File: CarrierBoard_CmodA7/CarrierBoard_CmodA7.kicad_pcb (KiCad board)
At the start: 2 copper layers, 76 x 85 mm, 69 parts, among them CN1 Mini-Fit_Jr._Header,_2_Circui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, J2 Conn1x26, U1 AZ1084CD-5.0, U2 Cmod_A7, U3 PMOD_GPIO, U4 PMOD_GPIO, U5 PMOD_GPIO, U6 PMOD_GPIO, U7 Conn1x21

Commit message: Arreglado Tira pines 1x22 a 1x21, cambiado el nivel de prioridad de los planos de cobre
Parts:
- U7: footprint Connector_PinSocket_2.54mm:PinSocket_1x22_P2.54mm_Vertical -> Connector_PinSocket_2.54mm:PinSocket_1x21_P2.54mm_Vertical
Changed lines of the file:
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@@
     )
   )
-  (footprint "Connector_PinSocket_2.54mm:PinSocket_1x22_P2.54mm_Vertical" (layer "F.Cu")
+  (footprint "Connector_PinSocket_2.54mm:PinSocket_1x21_P2.54mm_Vertical" (layer "F.Cu")
     (at 188.37 103.6 180)
-    (descr "Through hole straight socket strip, 1x22, 2.54mm pitch, single row (from Kicad 4.0.7), script generated")
-    (tags "Through hole socket strip THT 1x22 2.54mm single row")
+    (descr "Through hole straight socket strip, 1x21, 2.54mm pitch, single row (from Kicad 4.0.7), script generated")
+    (tags "Through hole socket strip THT 1x21 2.54mm single row")
     (property "Sheetfile" "CarrierBoard_CmodA7.kicad_sch")
     (property "Sheetname" "")
     (attr through_hole)
-    (fp_text reference "U7" (at 0 -2.77) (layer "F.SilkS")
-      (effects (font (size 1 1) (thickness 0.15)))
-    )
-    (fp_text value "Conn1x21" (at 0 56.11) (layer "F.Fab")
-      (effects (font (size 1 1) (thickness 0.15)))
-    )
-    (fp_text user "${REFERENCE}" (at 0 26.67 90) (layer "F.Fab")
+    (fp_text reference "U7" (at 0 -2.77 180) (layer "F.SilkS")
+      (effects (font (size 1 1) (thickness 0.15)))
+    )
+    (fp_text value "Conn1x21" (at 0 53.57 180) (layer "F.Fab")
+      (effects (font (size 1 1) (thickness 0.15)))
+    )
+    (fp_text user "${REFERENCE}" (at 0 25.4 270) (layer "F.Fab")
       (effects (font (size 1 1) (thickness 0.15)))
     )
     (fp_line (start 1.33 -1.33) (end 1.33 0) (layer "F.SilkS") (width 0.12))
+    (fp_line (start 0 -1.33) (end 1.33 -1.33) (layer "F.SilkS") (width 0.12))
+    (fp_line (start -1.33 1.27) (end -1.33 52.13) (layer "F.SilkS") (width 0.12))
+    (fp_line (start 1.33 1.27) (end 1.33 52.13) (layer "F.SilkS") (width 0.12))
     (fp_line (start -1.33 1.27) (end 1.33 1.27) (layer "F.SilkS") (width 0.12))
-    (fp_line (start 1.33 1.27) (end 1.33 54.67) (layer "F.SilkS") (width 0.12))
-    (fp_line (start 0 -1.33) (end 1.33 -1.33) (layer "F.SilkS") (width 0.12))
-    (fp_line (start -1.33 1.27) (end -1.33 54.67) (layer "F.SilkS") (width 0.12))
-    (fp_line (start -1.33 54.67) (end 1.33 54.67) (layer "F.SilkS") (width 0.12))
+    (fp_line (start -1.33 52.13) (end 1.33 52.13) (layer "F.SilkS") (width 0.12))
+    (fp_line (start 1.75 52.55) (end -1.8 52.55) (layer "F.CrtYd") (width 0.05))
     (fp_line (start -1.8 -1.8) (end 1.75 -1.8) (layer "F.CrtYd") (width 0.05))
-    (fp_line (start 1.75 55.1) (end -1.8 55.1) (layer "F.CrtYd") (width 0.05))
-    (fp_line (start 1.75 -1.8) (end 1.75 55.1) (layer "F.CrtYd") (width 0.05))
-    (fp_line (start -1.8 55.1) (end -1.8 -1.8) (layer "F.CrtYd") (width 0.05))
-    (fp_line (start -1.27 54.61) (end -1.27 -1.27) (layer "F.Fab") (width 0.1))
-    (fp_line (start 1.27 -0.635) (end 1.27 54.61) (layer "F.Fab") (width 0.1))
+    (fp_line (start -1.8 52.55) (end -1.8 -1.8) (layer "F.CrtYd") (width 0.05))
+    (fp_line (start 1.75 -1.8) (end 1.75 52.55) (layer "F.CrtYd") (width 0.05))
+    (fp_line (start 1.27 -0.635) (end 1.27 52.07) (layer "F.Fab") (width 0.1))
+    (fp_line (start 1.27 52.07) (end -1.27 52.07) (layer "F.Fab") (width 0.1))
+    (fp_line (start -1.27 52.07) (end -1.27 -1.27) (layer "F.Fab") (width 0.1))
+    (fp_line (start -1.27 -1.27) (end 0.635 -1.27) (layer "F.Fab") (width 0.1))
     (fp_line (start 0.635 -1.27) (end 1.27 -0.635) (layer "F.Fab") (width 0.1))
-    (fp_line (start 1.27 54.61) (end -1.27 54.61) (layer "F.Fab") (width 0.1))
-    (fp_line (start -1.27 -1.27) (end 0.635 -1.27) (layer "F.Fab") (width 0.1))
     (pad "1" thru_hole rect (at 0 0 180) (size 1.7 1.7) (drill 1) (layers *.Cu *.Mask)
       (net 6 "/IO1") (pinfunction "Pin_1") (pintype "passive"))
@@
     (pad "21" thru_hole oval (at 0 50.8 180) (size 1.7 1.7) (drill 1) (layers *.Cu *.Mask)
       (net 26 "/IO23") (pinfunction "Pin_21") (pintype "passive"))
-    (pad "22" thru_hole oval (at 0 53.34 180) (size 1.7 1.7) (drill 1) (layers *.Cu *.Mask))
-    (model "${KICAD6_3DMODEL_DIR}/Connector_PinSocket_2.54mm.3dshapes/PinSocket_1x22_P2.54mm_Vertical.wrl"
+    (model "${KICAD6_3DMODEL_DIR}/Connector_PinSocket_2.54mm.3dshapes/PinSocket_1x21_P2.54mm_Vertical.wrl"
       (offset (xyz 0 0 0))
       (scale (xyz 1 1 1))
@@
   )
   (zone (net 3) (net_name "+5VP") (layers F&B.Cu) (name "Thermal_Pad_Reg") (hatch edge 0.508)
+    (priority 1)
     (connect_pads yes (clearance 0.508))
     (min_thickness 0.254) (filled_areas_thickness no)
@@
     )
   )
-  (group "" (id b1729f9a-6241-4cf6-bc53-ffd2bc28c323)
-    (members
-      0e0ad59f-49c7-49e1-8181-4f4bccf85da4
-      0eba42d8-d7ba-40e9-9f63-a692f6ebec70
-      22800718-21a1-4d16-a6ef-62ea4e1a25d2
-      259f3bbe-b5fe-4a23-b8a5-4151f1c52b79
-      2838b2fd-e237-43d0-b648-62eafe5d8ba2
-      291f6aa0-1358-42fe-9954-b89ccd2c5246
-      29fa5c70-dc13-4d69-be92-fc44dbc9c06c
-      2a043446-b594-46bd-95f7-946ae3461b73
-      2a619e60-9cf4-4215-ac9c-6cd9b6a85a7e
-      360eba60-494e-4a5f-9bb9-79cd80a72cb8
-      40fa11de-0076-4b71-a33b-6abe07dfba23
-      7ce0ae94-595d-4e21-b198-de08b16fa989
-      8326c5bf-d461-4c7d-87c5-b33468c4e0e4
-      840035f9-760e-43d8-b42b-f557a49cae69
-      9749f2ba-8586-4a65-a776-3b84b130c532
-      9d6a82c1-0f4d-4bae-870a-6ea72ab488c3
-      bf55b3d2-0364-4479-8720-1aca56d25285
-      c7d1103e-0a6d-405e-84ef-a52ffdff7b0c
-      cd40a747-bd6a-4a01-aa00-0431b3021683
-      ce5b2749-5cdb-4128-9060-4f46bb280b28
-      d222c6dd-a6f9-4b4d-bd5a-f44cc391b25d
-      da97d51f-8207-40f6-b339-acda528d632e
-      dce1db7d-e8f9-4a59-b7c6-c640a8fc7761
-      e11136ec-0e76-4440-9929-ac565c57a1a3
-      e45e1b71-b8f0-4ba7-96b8-a7927cb62672
-      e6641f30-3cc7-49ac-bed5-4cb984494837
-      f2884391-266a-4503-8213-a5b50a2565c7
-      ff6428e0-e9e5-433c-ae23-83f42c1ecf89
-    )
-  )

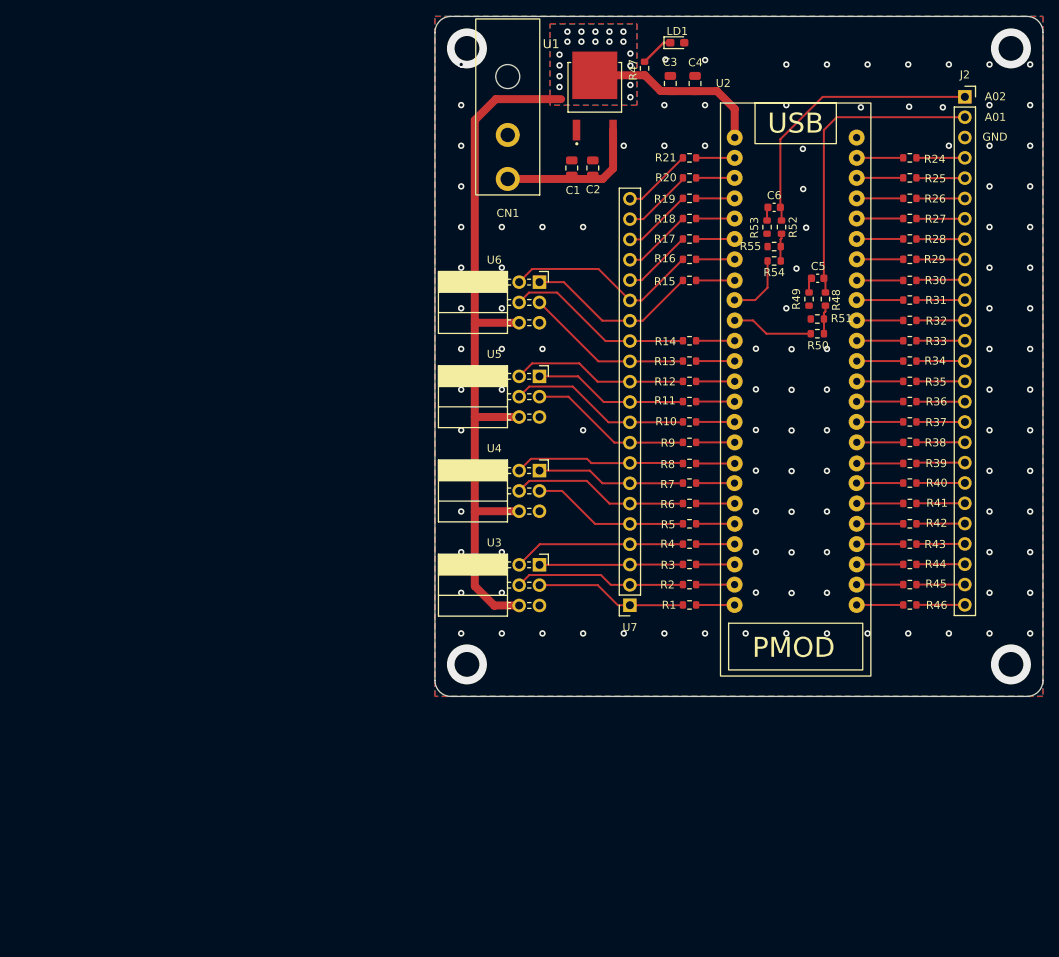
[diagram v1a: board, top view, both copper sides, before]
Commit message: arreglado divisor de tension y filtro del ADC.
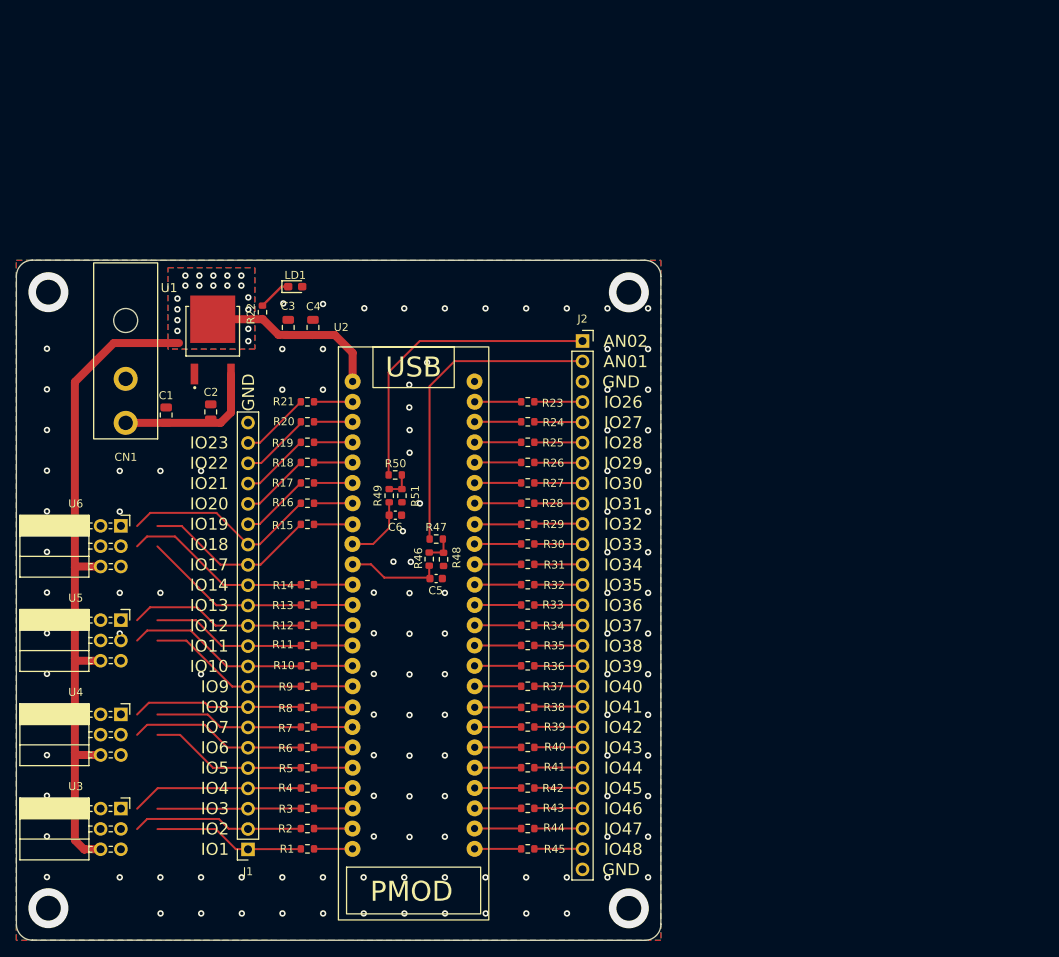
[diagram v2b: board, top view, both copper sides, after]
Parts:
- removed the R49 at (210.8, 65.3)
- removed R53: 845_P, Resistor_SMD:R_0603_1608Metric
- removed U7: Conn1x21, Connector_PinSocket_2.54mm:PinSocket_1x21_P2.54mm_Vertical
- added J1: Conn1x22, Connector_PinSocket_2.54mm:PinSocket_1x22_P2.54mm_Vertical, F.Cu at (140.6, 134.1)
- C1, C3: value 10uF -> Gen_C
- C2, C4: value 22uF -> Gen_C
- C5, C6: value 1nF -> Gen_C
- J2: value Conn1x26 -> Conn1x27; footprint Connector_PinSocket_2.54mm:PinSocket_1x26_P2.54mm_Vertical -> Connector_PinSocket_2.54mm:PinSocket_1x27_P2.54mm_Vertical
- moved C6 61.0 mm to (159.1, 92.3), turned to 0 degrees
- moved C5 60.7 mm to (164.2, 100.3), turned to 0 degrees
- moved U3 60.5 mm to (124.7, 129.0)
- moved U4 60.5 mm to (124.7, 117.2)
- moved U5 60.5 mm to (124.7, 105.5)
- moved U6 60.5 mm to (124.7, 93.7)
- moved R49 59.4 mm to (158.3, 89.9), turned to 90 degrees
- moved C1 59.4 mm to (130.4, 79.8)
- moved R46 59.2 mm to (163.3, 97.8), turned to 90 degrees
- moved J2 56.7 mm to (182.4, 70.6)
- moved R30 56.7 mm to (175.6, 95.9)
- moved R31 56.7 mm to (175.6, 98.5)
- moved R33 56.7 mm to (175.6, 103.6)
- moved R36 56.7 mm to (175.6, 111.2)
- moved R41 56.7 mm to (175.6, 123.9)
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- renumbered R47 to R22, R24 to R23, R25 to R24, R26 to R25, R27 to R26, R28 to R27, R29 to R28, R30 to R29, R31 to R30, R32 to R31, R33 to R32, R34 to R33, R35 to R34, R36 to R35, R37 to R36, R38 to R37, R39 to R38, R40 to R39, R41 to R40, R42 to R41, R43 to R42, R44 to R43, R45 to R44, R46 to R45, R48 to R46, R50 to R47, R51 to R48, R52 to R49, R54 to R50, R55 to R51
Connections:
- C5 pad 1: /AN01 -> /CH_A01
- C6 pad 1: /AN02 -> /CH_A02
- R46 pad 1: /AN01 -> /CH_A01
- R47 pad 2: /CH_A01 -> /AN01
- R49 pad 1: /AN02 -> /CH_A02
- R50 pad 2: /CH_A02 -> /AN02
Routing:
- net +5VP: track 116.2 -> 108.6 mm
- net GND: track 3.59 -> 0.00 mm, vias 116 -> 121
- net /AN02: track 35.5 -> 38.7 mm
- net /CH_A01: track 10.2 -> 12.0 mm
- net /AN01: track 38.7 -> 39.3 mm
- net /CH_A02: track 8.12 -> 8.63 mm
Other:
- board size 76 x 85 mm -> 80.6 x 85 mm
- board text added: "AN01"
- board text added: "AN02"
- board text added: "IO1"
- board text added: "IO10"
- board text added: "IO11"
- board text added: "IO12"
- board text added: "IO13"
- board text added: "IO14"
- board text added: "IO17"
- board text added: "IO18"
- board text added: "IO19"
- board text added: "IO2"
- board text added: "IO20"
- board text added: "IO21"
- board text added: "IO22"
- board text added: "IO23"
- board text added: "IO26"
- board text added: "IO27"
- board text added: "IO28"
- board text added: "IO29"
- board text added: "IO3"
- board text added: "IO30"
- board text added: "IO31"
- board text added: "IO32"
- board text added: "IO33"
- board text added: "IO34"
- board text added: "IO35"
- board text added: "IO36"
- board text added: "IO37"
- board text added: "IO38"
- board text added: "IO39"
- board text added: "IO4"
- board text added: "IO40"
- board text added: "IO41"
- board text added: "IO42"
- board text added: "IO43"
- board text added: "IO44"
- board text added: "IO45"
- board text added: "IO46"
- board text added: "IO47"
- board text added: "IO48"
- board text added: "IO5"
- board text added: "IO6"
- board text added: "IO7"
- board text added: "IO8"
- board text added: "IO9"
- board text removed: "A01"
- board text removed: "A02"

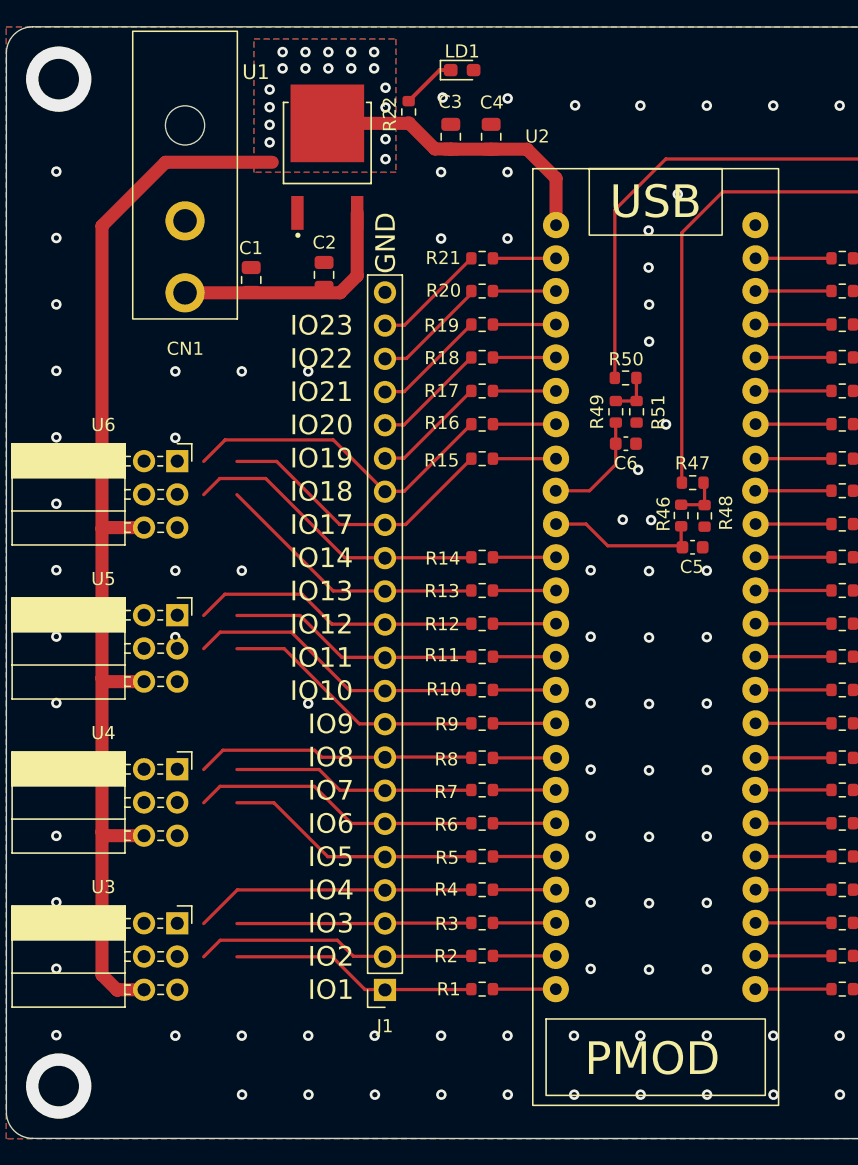
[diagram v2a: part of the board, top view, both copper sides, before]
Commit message: Retoques en la PCB, añadido info sobre el proyecto
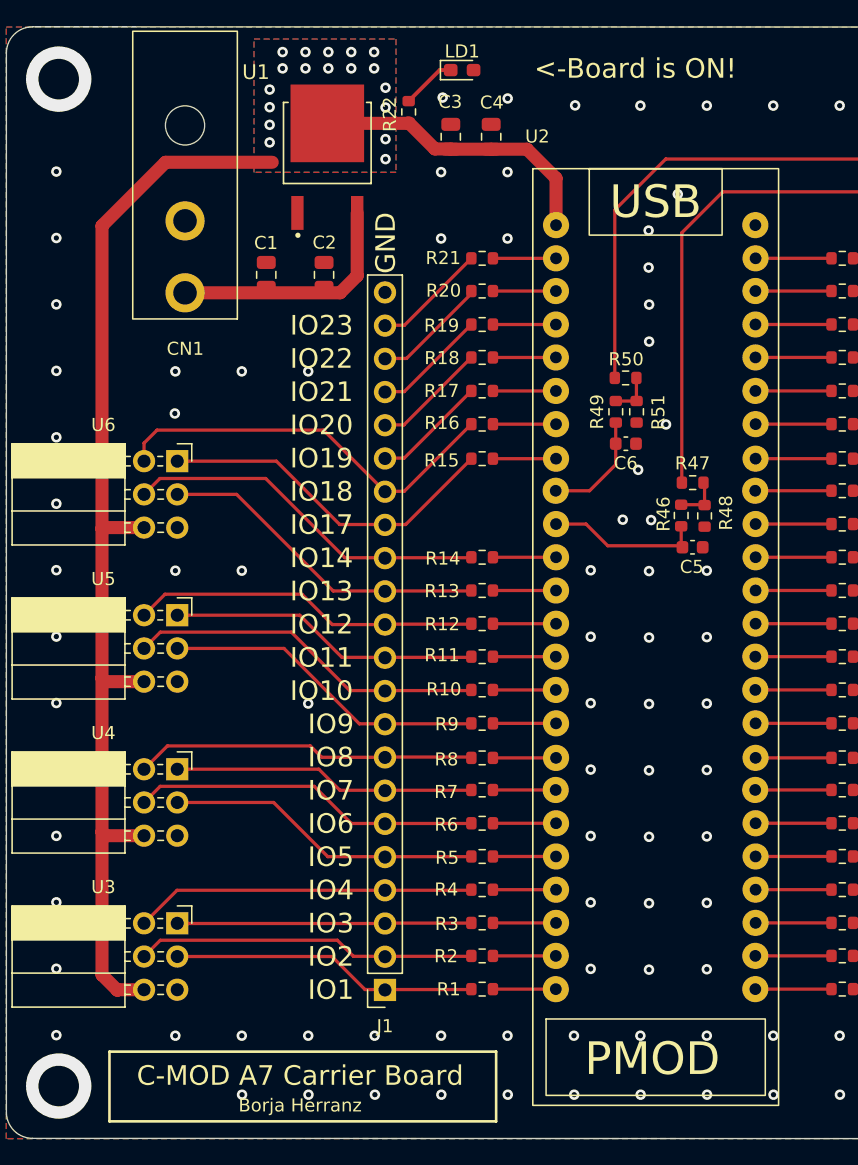
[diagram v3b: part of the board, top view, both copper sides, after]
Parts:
- moved C1 1.21 mm to (131.6, 79.4)
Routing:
- net /IO18: track 24.9 -> 30.9 mm
- net /IO8: track 21.3 -> 26.2 mm
- net /IO3: track 18.0 -> 22.6 mm
- net /IO12: track 22.8 -> 27.4 mm
- net /IO7: track 18.6 -> 23.2 mm
- net /IO5: track 19.6 -> 24.2 mm
- net /IO9: track 20.3 -> 24.9 mm
- net /IO1: track 19.0 -> 23.5 mm
- net /IO13: track 21.0 -> 25.6 mm
- net /IO11: track 19.3 -> 23.8 mm
- net /IO17: track 22.0 -> 26.6 mm
- net /IO4: track 21.5 -> 26.1 mm
- net /IO6: track 22.2 -> 26.7 mm
- net /IO2: track 21.5 -> 26.1 mm
- net /IO14: track 23.5 -> 28.1 mm
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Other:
- board text added: "<-Board is ON!"
- board text added: "Borja Herranz"
- board text added: "https://github.com/herranz/CmodA7_CarrierBoard"

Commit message: Arreglado BoM y esquemas
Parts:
- C1, C3: value Gen_C -> 10uF
- C2, C4: value Gen_C -> 100nF
- C5, C6: value Gen_C -> 1nF
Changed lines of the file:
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@@
       (effects (font (size 1 1) (thickness 0.15)))
     )
-    (fp_text value "Gen_C" (at 0 1.43) (layer "F.Fab")
+    (fp_text value "1nF" (at 0 1.43) (layer "F.Fab")
       (effects (font (size 1 1) (thickness 0.15)))
     )
@@
       (effects (font (size 1 1) (thickness 0.15)))
     )
-    (fp_text value "Gen_C" (at 0 1.68 90) (layer "F.Fab")
+    (fp_text value "100nF" (at 0 1.68 90) (layer "F.Fab")
       (effects (font (size 1 1) (thickness 0.15)))
     )
@@
       (effects (font (size 1 1) (thickness 0.15)))
     )
-    (fp_text value "Gen_C" (at 0 1.68 90) (layer "F.Fab")
+    (fp_text value "10uF" (at 0 1.68 90) (layer "F.Fab")
       (effects (font (size 1 1) (thickness 0.15)))
     )
@@
       (effects (font (size 1 1) (thickness 0.15)))
     )
-    (fp_text value "Gen_C" (at 0 1.68 90) (layer "F.Fab")
+    (fp_text value "100nF" (at 0 1.68 90) (layer "F.Fab")
       (effects (font (size 1 1) (thickness 0.15)))
     )
@@
       (effects (font (size 1 1) (thickness 0.15)))
     )
-    (fp_text value "Gen_C" (at 0 1.68 90) (layer "F.Fab")
+    (fp_text value "10uF" (at 0 1.68 90) (layer "F.Fab")
       (effects (font (size 1 1) (thickness 0.15)))
     )
@@
       (effects (font (size 1 1) (thickness 0.15)))
     )
-    (fp_text value "Gen_C" (at 0 1.43) (layer "F.Fab")
-      (effects (font (size 1 1) (thickness 0.15)))
-    )
+    (fp_text value "1nF" (at 0 1.43) (layer "F.Fab")
+      (effects (font (size 1 1) (thickness 0.15)))
+    )
